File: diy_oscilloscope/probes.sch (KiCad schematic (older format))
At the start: 49 parts

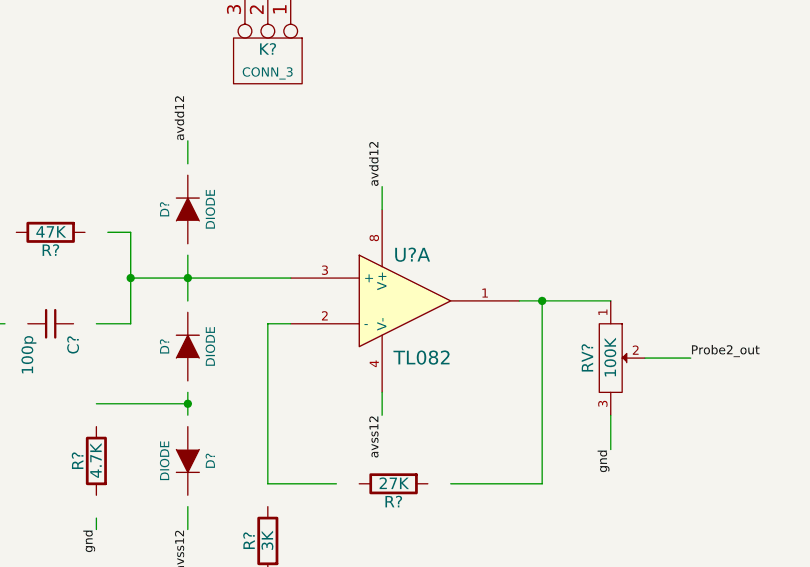
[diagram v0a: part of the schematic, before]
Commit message: Preparation for single sided PCB.
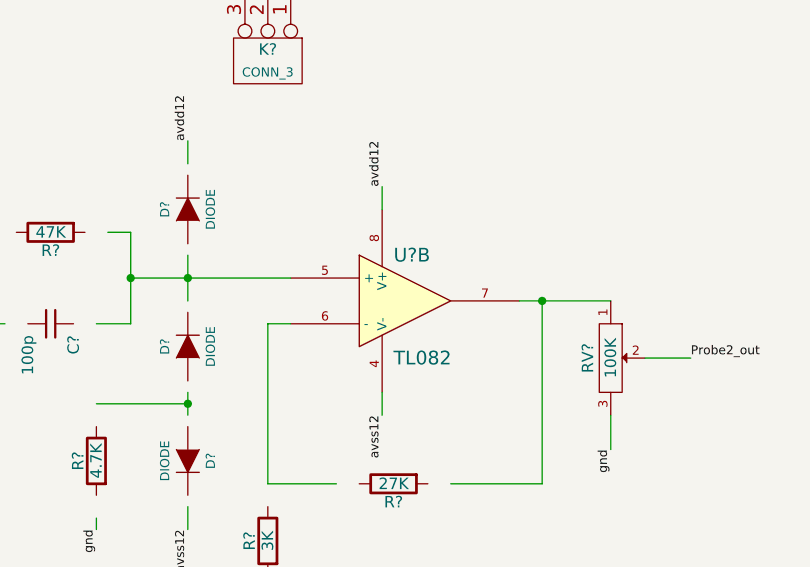
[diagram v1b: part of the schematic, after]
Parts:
- C? (x14): footprint (none) -> c_1206
- D? (x2): footprint (none) -> LED-3MM
- R? (x10): footprint (none) -> r_1206
- R? (x2): footprint (none) -> R1
- T?: footprint (none) -> ANG6VA/15V+15V
- U? (x2): footprint (none) -> DIP-8_300
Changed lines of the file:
@@
-EESchema Schematic File Version 2  date Fri 09 Nov 2012 02:12:44 PM EET
+EESchema Schematic File Version 2  date Sat 10 Nov 2012 07:59:52 PM EET
 LIBS:power
 LIBS:device
@@
 LIBS:diy_oscilloscope
 LIBS:probes-cache
-EELAYER 25  0
+EELAYER 27 0
 EELAYER END
-$Descr A4 11700 8267
+$Descr A4 11693 8268
 encoding utf-8
 Sheet 1 1
 Title "PC oscilloscope probes 150 V max / 1x and 10x for xoscope"
-Date "9 nov 2012"
+Date "10 nov 2012"
 Rev "v1.0"
 Comp ""
@@
 F 0 "D?" H 3950 6900 50  0000 C CNN
 F 1 "LED" H 3950 6700 50  0000 C CNN
+F 2 "LED-3MM" H 3950 6800 60  0001 C CNN
 	1    3950 6800
 	0    -1   -1   0
@@
 F 0 "R?" V 4330 7050 50  0000 C CNN
 F 1 "1.5K" V 4250 7050 50  0000 C CNN
+F 2 "r_1206" H 4250 7050 60  0001 C CNN
 	1    4250 7050
 	0    -1   -1   0
@@
 F 0 "R?" V 4330 6200 50  0000 C CNN
 F 1 "1.5K" V 4250 6200 50  0000 C CNN
+F 2 "r_1206" H 4250 6200 60  0001 C CNN
 	1    4250 6200
 	0    -1   -1   0
@@
 F 0 "D?" H 3950 6050 50  0000 C CNN
 F 1 "LED" H 3950 5850 50  0000 C CNN
+F 2 "LED-3MM" H 3950 5950 60  0001 C CNN
 	1    3950 5950
 	0    1    1    0
@@
 F 0 "C?" H 3550 6900 50  0000 L CNN
 F 1 "10u" H 3550 6700 50  0000 L CNN
+F 2 "c_1206" H 3500 6800 60  0001 C CNN
 	1    3500 6800
 	-1   0    0    1
@@
 F 0 "T?" H 2150 2150 70  0000 C CNN
 F 1 "BULTRAF2.3VA/12V+12V" H 2150 1150 70  0000 C CNN
+F 2 "ANG6VA/15V+15V" H 2150 1650 60  0001 C CNN
 	1    2150 1650
 	1    0    0    -1
@@
 F 0 "C?" H 1650 6900 50  0000 L CNN
 F 1 "10u" H 1650 6700 50  0000 L CNN
+F 2 "c_1206" H 1600 6800 60  0001 C CNN
 	1    1600 6800
 	-1   0    0    1
@@
 F 0 "C?" H 3550 6050 50  0000 L CNN
 F 1 "10u" H 3550 5850 50  0000 L CNN
+F 2 "c_1206" H 3500 5950 60  0001 C CNN
 	1    3500 5950
 	-1   0    0    1
@@
 F 0 "C?" H 1650 6050 50  0000 L CNN
 F 1 "10u" H 1650 5850 50  0000 L CNN
+F 2 "c_1206" H 1600 5950 60  0001 C CNN
 	1    1600 5950
 	-1   0    0    1
@@
 F 0 "C?" H 3250 6900 50  0000 L CNN
 F 1 "100n" H 3250 6700 50  0000 L CNN
+F 2 "c_1206" H 3200 6800 60  0001 C CNN
 	1    3200 6800
 	-1   0    0    1
@@
 F 0 "C?" H 2050 6900 50  0000 L CNN
 F 1 "330n" H 2050 6700 50  0000 L CNN
+F 2 "c_1206" H 2000 6800 60  0001 C CNN
 	1    2000 6800
 	-1   0    0    1
@@
 F 0 "C?" H 3250 6050 50  0000 L CNN
 F 1 "100n" H 3250 5850 50  0000 L CNN
+F 2 "c_1206" H 3200 5950 60  0001 C CNN
 	1    3200 5950
 	-1   0    0    1
@@
 F 0 "C?" H 2050 6050 50  0000 L CNN
 F 1 "330n" H 2050 5850 50  0000 L CNN
+F 2 "c_1206" H 2000 5950 60  0001 C CNN
 	1    2000 5950
 	-1   0    0    1
@@
 $Comp
 L TL082 U?
-U 1 1 509CE234
+U 2 1 509CE234
 P 8000 4500
 F 0 "U?" H 7950 4700 60  0000 L CNN
 F 1 "TL082" H 7950 4250 60  0000 L CNN
-	1    8000 4500
+F 2 "DIP-8_300" H 8000 4500 60  0001 C CNN
+	2    8000 4500
 	1    0    0    -1
 $EndComp
@@
 F 0 "R?" V 8030 5300 50  0000 C CNN
 F 1 "27K" V 7950 5300 50  0000 C CNN
+F 2 "r_1206" H 7950 5300 60  0001 C CNN
 	1    7950 5300
 	0    1    1    0
@@
 F 0 "R?" V 7480 5550 50  0000 C CNN
 F 1 "3K" V 7400 5550 50  0000 C CNN
+F 2 "r_1206" H 7400 5550 60  0001 C CNN
 	1    7400 5550
 	-1   0    0    1
@@
 F 0 "R?" V 6530 4200 50  0000 C CNN
 F 1 "47K" V 6450 4200 50  0000 C CNN
+F 2 "R1" H 6450 4200 60  0001 C CNN
 	1    6450 4200
 	0    1    1    0
@@
 F 0 "C?" H 6500 4700 50  0000 L CNN
 F 1 "100p" H 6500 4500 50  0000 L CNN
+F 2 "c_1206" H 6450 4600 60  0001 C CNN
 	1    6450 4600
 	0    1    1    0
@@
 F 0 "R?" V 6730 5200 50  0000 C CNN
 F 1 "4.7K" V 6650 5200 50  0000 C CNN
+F 2 "r_1206" H 6650 5200 60  0001 C CNN
 	1    6650 5200
 	-1   0    0    1
@@
 F 0 "R?" V 5580 4650 50  0000 C CNN
 F 1 "1M" V 5500 4650 50  0000 C CNN
+F 2 "r_1206" H 5500 4650 60  0001 C CNN
 	1    5500 4650
 	-1   0    0    1
@@
 F 0 "C?" H 5900 4700 50  0000 L CNN
 F 1 "20p" H 5900 4500 50  0000 L CNN
+F 2 "c_1206" H 5850 4600 60  0001 C CNN
 	1    5850 4600
 	-1   0    0    1
@@
 F 0 "C?" H 5150 4500 50  0000 L CNN
 F 1 "10n" H 5150 4300 50  0000 L CNN
+F 2 "c_1206" H 5100 4400 60  0001 C CNN
 	1    5100 4400
 	0    1    1    0
@@
 F 0 "C?" H 5150 1750 50  0000 L CNN
 F 1 "10n" H 5150 1550 50  0000 L CNN
+F 2 "c_1206" H 5100 1650 60  0001 C CNN
 	1    5100 1650
 	0    1    1    0
@@
 F 0 "C?" H 5900 1950 50  0000 L CNN
 F 1 "20p" H 5900 1750 50  0000 L CNN
+F 2 "c_1206" H 5850 1850 60  0001 C CNN
 	1    5850 1850
 	-1   0    0    1
@@
 F 0 "R?" V 5580 1900 50  0000 C CNN
 F 1 "1M" V 5500 1900 50  0000 C CNN
+F 2 "r_1206" H 5500 1900 60  0001 C CNN
 	1    5500 1900
 	-1   0    0    1
@@
 F 0 "R?" V 6730 2450 50  0000 C CNN
 F 1 "4.7K" V 6650 2450 50  0000 C CNN
+F 2 "r_1206" H 6650 2450 60  0001 C CNN
 	1    6650 2450
 	-1   0    0    1
@@
 F 0 "C?" H 6500 1950 50  0000 L CNN
 F 1 "100p" H 6500 1750 50  0000 L CNN
+F 2 "c_1206" H 6450 1850 60  0001 C CNN
 	1    6450 1850
 	0    1    1    0
@@
 F 0 "R?" V 6530 1450 50  0000 C CNN
 F 1 "47K" V 6450 1450 50  0000 C CNN
+F 2 "R1" H 6450 1450 60  0001 C CNN
 	1    6450 1450
 	0    1    1    0
@@
 F 0 "R?" V 7480 2800 50  0000 C CNN
 F 1 "3K" V 7400 2800 50  0000 C CNN
+F 2 "r_1206" H 7400 2800 60  0001 C CNN
 	1    7400 2800
 	-1   0    0    1
@@
 F 0 "R?" V 8030 2550 50  0000 C CNN
 F 1 "27K" V 7950 2550 50  0000 C CNN
+F 2 "r_1206" H 7950 2550 60  0001 C CNN
 	1    7950 2550
 	0    1    1    0
@@
 F 0 "U?" H 7950 1950 60  0000 L CNN
 F 1 "TL082" H 7950 1500 60  0000 L CNN
+F 2 "DIP-8_300" H 8000 1750 60  0001 C CNN
 	1    8000 1750
 	1    0    0    -1

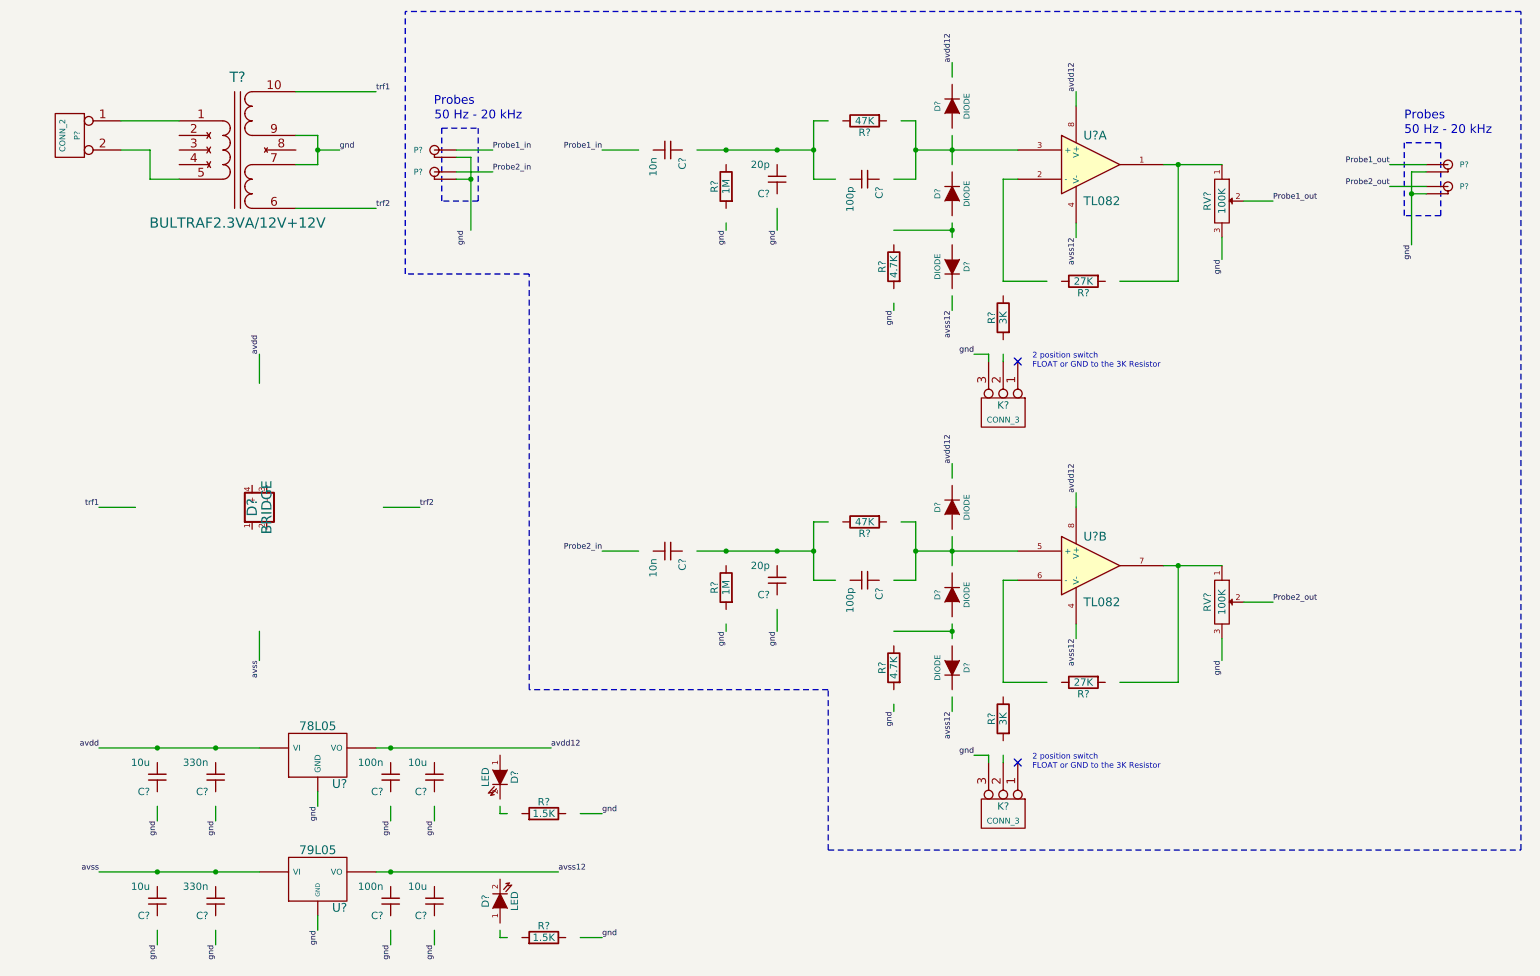
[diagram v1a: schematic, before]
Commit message: Started routing of the pcb. Should be single sided pcb.
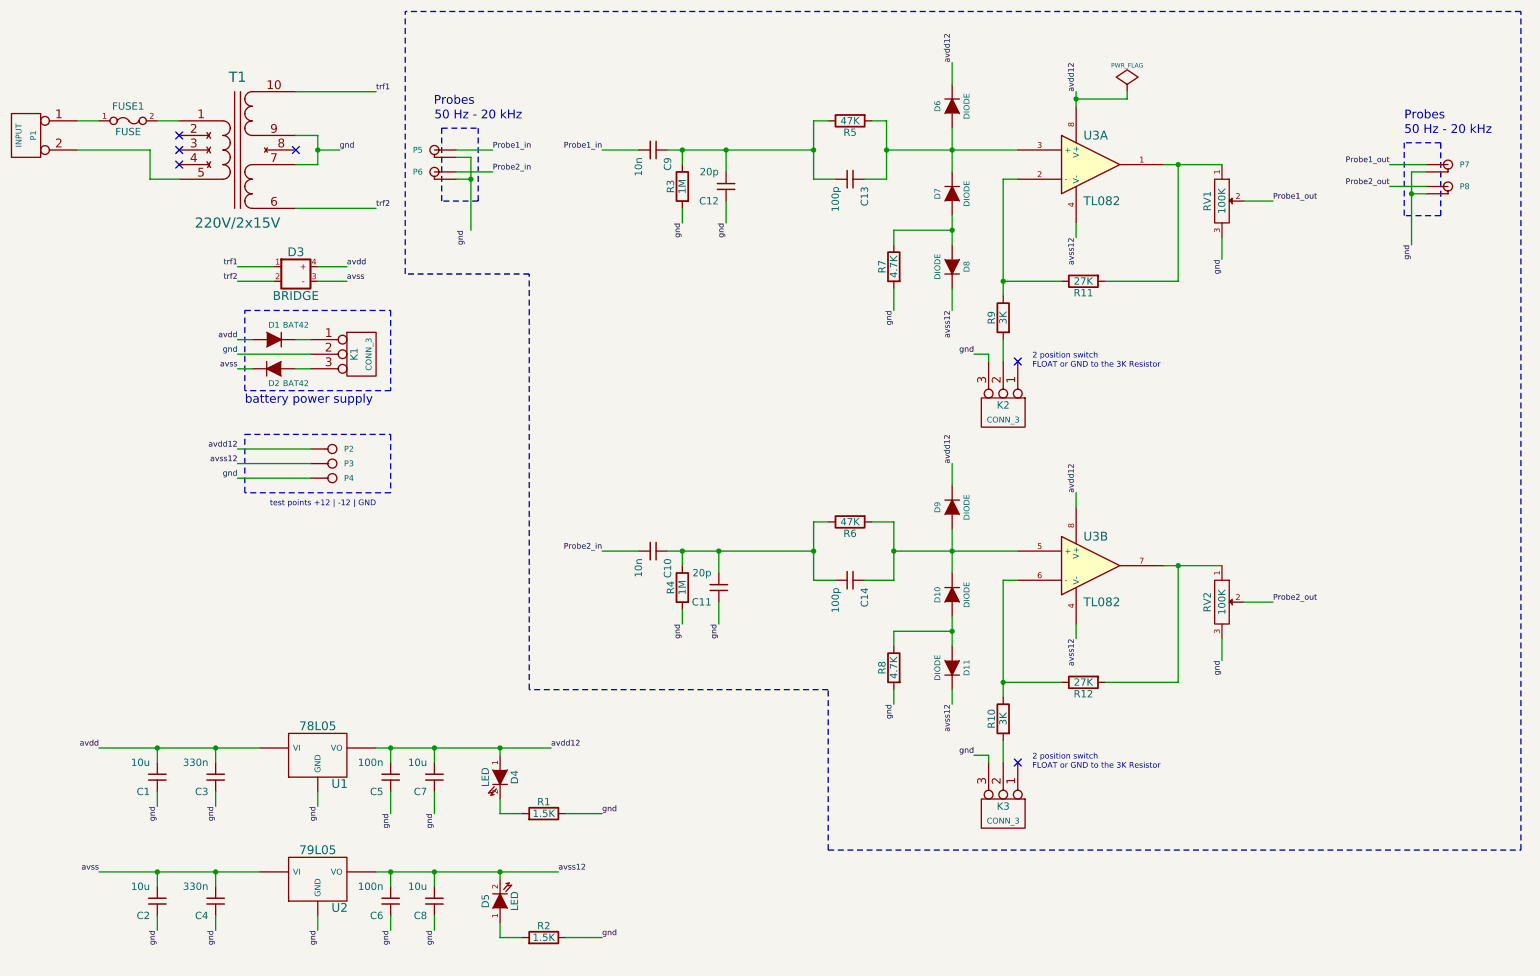
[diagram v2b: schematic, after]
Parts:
- removed D?: BRIDGE, symbol BRIDGE
- removed P?: CONN_2, symbol CONN_2
- removed T?: BULTRAF2.3VA/12V+12V, ANG6VA/15V+15V, symbol TRANSFO2
- removed U?: 79L05, symbol 79L05
- added D1, D2: BAT42, micromelf, symbol DIODE
- added D3: BRIDGE, bridge_wob, symbol BRIDGE
- added FUSE1: FUSE, fuse_holder_CQ-2, symbol FUSE
- added K1: CONN_3, mors_3p, symbol CONN_3
- added P1: INPUT, mors_2p, symbol CONN_2
- added P2, P3, P4: CONN_1, testpoint_2mm5, symbol CONN_1
- added T1: 220V/2x15V, TRF_ANG6VA/15V+5V, symbol TRANSFO2
- added U2: 79L05, TO92, symbol 78L05
- D10, D11, D6, D7, D8, D9: renamed from D?; footprint (none) -> micromelf
- D4, D5: renamed from D?; footprint LED-3MM -> led_3mm_red
- K2, K3: renamed from K?; footprint (none) -> pin_strip_3
- P5, P6, P7, P8: renamed from P?; footprint (none) -> RCA Connector F / PCB 90deg
- R5, R6: renamed from R?; footprint R1 -> rc05_vert
- RV1, RV2: renamed from RV?; footprint (none) -> trimmer_64w
- U1: renamed from U?; footprint (none) -> TO92
- gave numbers to parts that had none: 25
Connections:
- wire segments 104 -> 131
- no-connect marks 2 -> 6
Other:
- note added: "battery power supply"
- note added: "test points +12 | -12 | GND"
- moved on the sheet: C10, C11, C12, C13, C14, C9, R3, R4, R5, R6
